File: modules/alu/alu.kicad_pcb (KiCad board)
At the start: 2 copper layers, 7 parts, among them Q1 2N3906, Q2 2N3904, Q3 2N3904

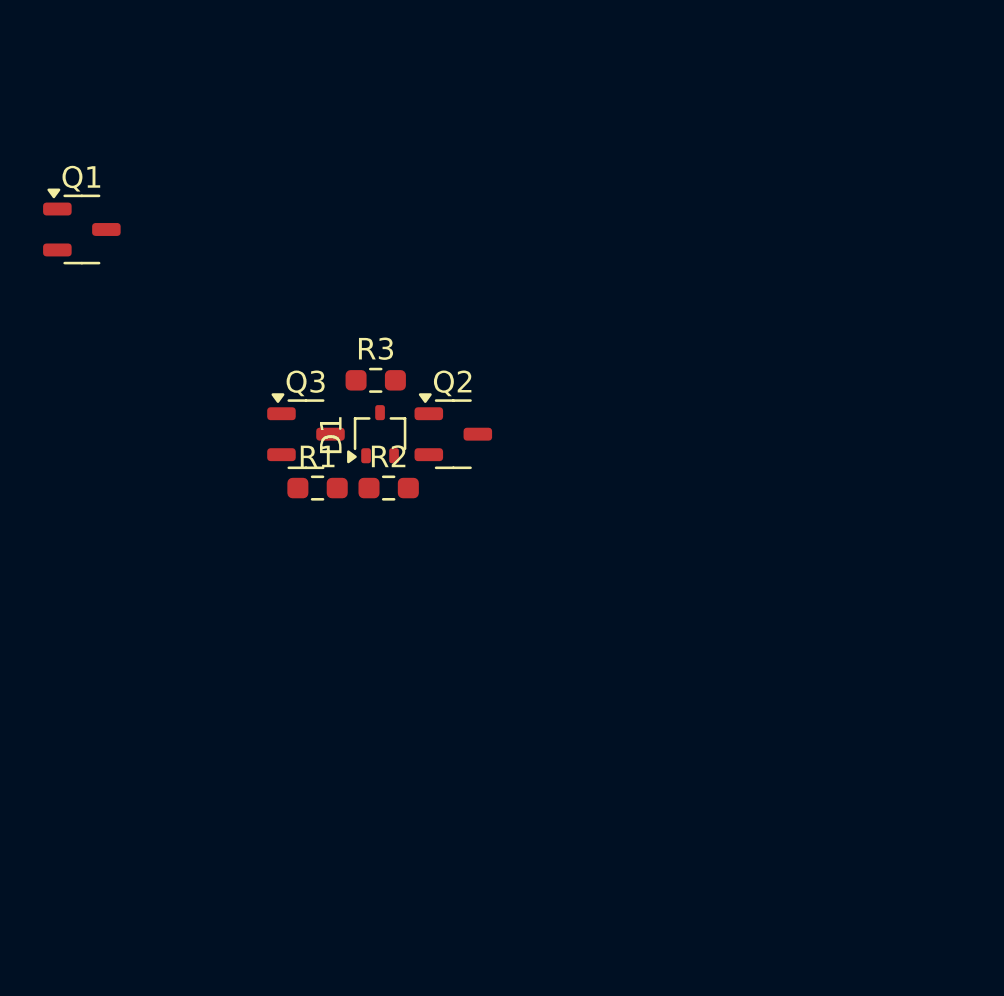
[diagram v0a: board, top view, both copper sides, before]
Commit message: Much work towards an actual ALU bit-cell.
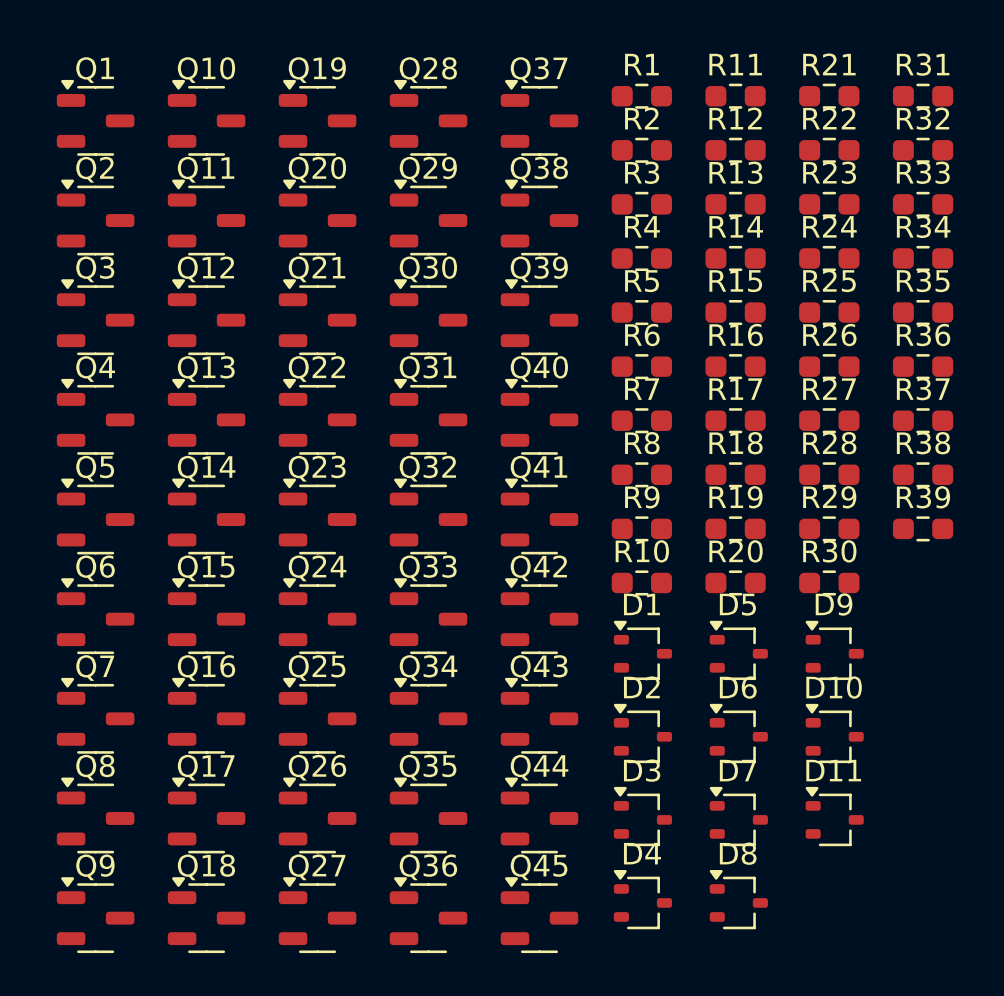
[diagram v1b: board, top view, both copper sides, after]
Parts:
- added D10: BAT54W, Package_TO_SOT_SMD:SOT-323_SC-70, F.Cu at (154.2, 96.6)
- added D11: BAT54W, Package_TO_SOT_SMD:SOT-323_SC-70, F.Cu at (154.2, 100.5)
- added D2: BAT54W, Package_TO_SOT_SMD:SOT-323_SC-70, F.Cu at (145.3, 96.6)
- added D3: BAT54W, Package_TO_SOT_SMD:SOT-323_SC-70, F.Cu at (145.3, 100.5)
- added D4: BAT54W, Package_TO_SOT_SMD:SOT-323_SC-70, F.Cu at (145.3, 104.4)
- added D5: BAT54W, Package_TO_SOT_SMD:SOT-323_SC-70, F.Cu at (149.8, 92.8)
- added D6: BAT54W, Package_TO_SOT_SMD:SOT-323_SC-70, F.Cu at (149.8, 96.6)
- added D7: BAT54W, Package_TO_SOT_SMD:SOT-323_SC-70, F.Cu at (149.8, 100.5)
- added D8: BAT54W, Package_TO_SOT_SMD:SOT-323_SC-70, F.Cu at (149.8, 104.4)
- added D9: BAT54W, Package_TO_SOT_SMD:SOT-323_SC-70, F.Cu at (154.2, 92.8)
- added Q10: 2N3906, Package_TO_SOT_SMD:SOT-23-3, F.Cu at (125.0, 68.1)
- added Q11: 2N3904, Package_TO_SOT_SMD:SOT-23-3, F.Cu at (125.0, 72.7)
- added Q12: 2N3904, Package_TO_SOT_SMD:SOT-23-3, F.Cu at (125.0, 77.3)
- added Q13: 2N3904, Package_TO_SOT_SMD:SOT-23-3, F.Cu at (125.0, 81.9)
- added Q14: 2N3904, Package_TO_SOT_SMD:SOT-23-3, F.Cu at (125.0, 86.6)
- added Q15: 2N3904, Package_TO_SOT_SMD:SOT-23-3, F.Cu at (125.0, 91.2)
- added Q16: 2N3904, Package_TO_SOT_SMD:SOT-23-3, F.Cu at (125.0, 95.8)
- added Q17: 2N3904, Package_TO_SOT_SMD:SOT-23-3, F.Cu at (125.0, 100.4)
- added Q18: 2N3906, Package_TO_SOT_SMD:SOT-23-3, F.Cu at (125.0, 105.1)
- added Q19: 2N3904, Package_TO_SOT_SMD:SOT-23-3, F.Cu at (130.2, 68.1)
- added Q20: 2N3906, Package_TO_SOT_SMD:SOT-23-3, F.Cu at (130.2, 72.7)
- added Q21: 2N3904, Package_TO_SOT_SMD:SOT-23-3, F.Cu at (130.2, 77.3)
- added Q22: 2N3906, Package_TO_SOT_SMD:SOT-23-3, F.Cu at (130.2, 81.9)
- added Q23: 2N3904, Package_TO_SOT_SMD:SOT-23-3, F.Cu at (130.2, 86.6)
- added Q24: 2N3906, Package_TO_SOT_SMD:SOT-23-3, F.Cu at (130.2, 91.2)
- added Q25: 2N3906, Package_TO_SOT_SMD:SOT-23-3, F.Cu at (130.2, 95.8)
- added Q26: 2N3906, Package_TO_SOT_SMD:SOT-23-3, F.Cu at (130.2, 100.4)
- added Q27: 2N3906, Package_TO_SOT_SMD:SOT-23-3, F.Cu at (130.2, 105.1)
- added Q28: 2N3904, Package_TO_SOT_SMD:SOT-23-3, F.Cu at (135.3, 68.1)
- added Q29: 2N3904, Package_TO_SOT_SMD:SOT-23-3, F.Cu at (135.3, 72.7)
- added Q30: 2N3904, Package_TO_SOT_SMD:SOT-23-3, F.Cu at (135.3, 77.3)
- added Q31: 2N3906, Package_TO_SOT_SMD:SOT-23-3, F.Cu at (135.3, 81.9)
- added Q32: 2N3906, Package_TO_SOT_SMD:SOT-23-3, F.Cu at (135.3, 86.6)
- added Q33: 2N3904, Package_TO_SOT_SMD:SOT-23-3, F.Cu at (135.3, 91.2)
- added Q34: 2N3904, Package_TO_SOT_SMD:SOT-23-3, F.Cu at (135.3, 95.8)
- added Q35: 2N3906, Package_TO_SOT_SMD:SOT-23-3, F.Cu at (135.3, 100.4)
- added Q36: 2N3904, Package_TO_SOT_SMD:SOT-23-3, F.Cu at (135.3, 105.1)
- added Q37: 2N3906, Package_TO_SOT_SMD:SOT-23-3, F.Cu at (140.5, 68.1)
- added Q38: 2N3906, Package_TO_SOT_SMD:SOT-23-3, F.Cu at (140.5, 72.7)
- added Q39: 2N3906, Package_TO_SOT_SMD:SOT-23-3, F.Cu at (140.5, 77.3)
- added Q4: 2N3904, Package_TO_SOT_SMD:SOT-23-3, F.Cu at (119.9, 81.9)
- added Q40: 2N3906, Package_TO_SOT_SMD:SOT-23-3, F.Cu at (140.5, 81.9)
- added Q41: 2N3906, Package_TO_SOT_SMD:SOT-23-3, F.Cu at (140.5, 86.6)
- added Q42: 2N3906, Package_TO_SOT_SMD:SOT-23-3, F.Cu at (140.5, 91.2)
- added Q43: 2N3904, Package_TO_SOT_SMD:SOT-23-3, F.Cu at (140.5, 95.8)
- added Q44: 2N3904, Package_TO_SOT_SMD:SOT-23-3, F.Cu at (140.5, 100.4)
- added Q45: 2N3904, Package_TO_SOT_SMD:SOT-23-3, F.Cu at (140.5, 105.1)
- added Q5: 2N3904, Package_TO_SOT_SMD:SOT-23-3, F.Cu at (119.9, 86.6)
- added Q6: 2N3904, Package_TO_SOT_SMD:SOT-23-3, F.Cu at (119.9, 91.2)
- added Q7: 2N3906, Package_TO_SOT_SMD:SOT-23-3, F.Cu at (119.9, 95.8)
- added Q8: 2N3906, Package_TO_SOT_SMD:SOT-23-3, F.Cu at (119.9, 100.4)
- added Q9: 2N3906, Package_TO_SOT_SMD:SOT-23-3, F.Cu at (119.9, 105.1)
- added R10: 520, Resistor_SMD:R_0603_1608Metric_Pad0.98x0.95mm_HandSolder, F.Cu at (145.2, 89.5)
- added R11: 220, Resistor_SMD:R_0603_1608Metric_Pad0.98x0.95mm_HandSolder, F.Cu at (149.6, 66.9)
- added R12: 220, Resistor_SMD:R_0603_1608Metric_Pad0.98x0.95mm_HandSolder, F.Cu at (149.6, 69.4)
- added R13: 220, Resistor_SMD:R_0603_1608Metric_Pad0.98x0.95mm_HandSolder, F.Cu at (149.6, 71.9)
- added R14: 220, Resistor_SMD:R_0603_1608Metric_Pad0.98x0.95mm_HandSolder, F.Cu at (149.6, 74.4)
- added R15: 100, Resistor_SMD:R_0603_1608Metric_Pad0.98x0.95mm_HandSolder, F.Cu at (149.6, 77.0)
- added R16: 100, Resistor_SMD:R_0603_1608Metric_Pad0.98x0.95mm_HandSolder, F.Cu at (149.6, 79.5)
- added R17: 220, Resistor_SMD:R_0603_1608Metric_Pad0.98x0.95mm_HandSolder, F.Cu at (149.6, 82.0)
- added R18: 220, Resistor_SMD:R_0603_1608Metric_Pad0.98x0.95mm_HandSolder, F.Cu at (149.6, 84.5)
- added R19: 220, Resistor_SMD:R_0603_1608Metric_Pad0.98x0.95mm_HandSolder, F.Cu at (149.6, 87.0)
- added R20: 220, Resistor_SMD:R_0603_1608Metric_Pad0.98x0.95mm_HandSolder, F.Cu at (149.6, 89.5)
- added R21: 100, Resistor_SMD:R_0603_1608Metric_Pad0.98x0.95mm_HandSolder, F.Cu at (153.9, 66.9)
- added R22: 100, Resistor_SMD:R_0603_1608Metric_Pad0.98x0.95mm_HandSolder, F.Cu at (153.9, 69.4)
- added R23: 520, Resistor_SMD:R_0603_1608Metric_Pad0.98x0.95mm_HandSolder, F.Cu at (153.9, 71.9)
- added R24: 220, Resistor_SMD:R_0603_1608Metric_Pad0.98x0.95mm_HandSolder, F.Cu at (153.9, 74.4)
- added R25: 220, Resistor_SMD:R_0603_1608Metric_Pad0.98x0.95mm_HandSolder, F.Cu at (153.9, 77.0)
- added R26: 100, Resistor_SMD:R_0603_1608Metric_Pad0.98x0.95mm_HandSolder, F.Cu at (153.9, 79.5)
- added R27: 220, Resistor_SMD:R_0603_1608Metric_Pad0.98x0.95mm_HandSolder, F.Cu at (153.9, 82.0)
- added R28: 220, Resistor_SMD:R_0603_1608Metric_Pad0.98x0.95mm_HandSolder, F.Cu at (153.9, 84.5)
- added R29: 220, Resistor_SMD:R_0603_1608Metric_Pad0.98x0.95mm_HandSolder, F.Cu at (153.9, 87.0)
- added R30: 220, Resistor_SMD:R_0603_1608Metric_Pad0.98x0.95mm_HandSolder, F.Cu at (153.9, 89.5)
- added R31: 100, Resistor_SMD:R_0603_1608Metric_Pad0.98x0.95mm_HandSolder, F.Cu at (158.3, 66.9)
- added R32: 100, Resistor_SMD:R_0603_1608Metric_Pad0.98x0.95mm_HandSolder, F.Cu at (158.3, 69.4)
- added R33: 520, Resistor_SMD:R_0603_1608Metric_Pad0.98x0.95mm_HandSolder, F.Cu at (158.3, 71.9)
- added R34: 220, Resistor_SMD:R_0603_1608Metric_Pad0.98x0.95mm_HandSolder, F.Cu at (158.3, 74.4)
- added R35: 220, Resistor_SMD:R_0603_1608Metric_Pad0.98x0.95mm_HandSolder, F.Cu at (158.3, 77.0)
- added R36: 100, Resistor_SMD:R_0603_1608Metric_Pad0.98x0.95mm_HandSolder, F.Cu at (158.3, 79.5)
- added R37: 220, Resistor_SMD:R_0603_1608Metric_Pad0.98x0.95mm_HandSolder, F.Cu at (158.3, 82.0)
- added R38: 220, Resistor_SMD:R_0603_1608Metric_Pad0.98x0.95mm_HandSolder, F.Cu at (158.3, 84.5)
- added R39: 100, Resistor_SMD:R_0603_1608Metric_Pad0.98x0.95mm_HandSolder, F.Cu at (158.3, 87.0)
- added R4: 220, Resistor_SMD:R_0603_1608Metric_Pad0.98x0.95mm_HandSolder, F.Cu at (145.2, 74.4)
- added R5: 220, Resistor_SMD:R_0603_1608Metric_Pad0.98x0.95mm_HandSolder, F.Cu at (145.2, 77.0)
- added R6: 220, Resistor_SMD:R_0603_1608Metric_Pad0.98x0.95mm_HandSolder, F.Cu at (145.2, 79.5)
- added R7: 100, Resistor_SMD:R_0603_1608Metric_Pad0.98x0.95mm_HandSolder, F.Cu at (145.2, 82.0)
- added R8: 100, Resistor_SMD:R_0603_1608Metric_Pad0.98x0.95mm_HandSolder, F.Cu at (145.2, 84.5)
- added R9: 520, Resistor_SMD:R_0603_1608Metric_Pad0.98x0.95mm_HandSolder, F.Cu at (145.2, 87.0)
- Q1: value 2N3906 -> 2N3904
- R1: value 600 -> 10k
- R2: value 300 -> 10k
- R3: value 300 -> 220
- moved R1 23.6 mm to (145.2, 66.9)
- moved R2 19.6 mm to (145.2, 69.4)
- moved Q2 19.3 mm to (119.9, 72.7)
- moved D1 15.9 mm to (145.3, 92.8), turned to 0 degrees
- moved R3 14.8 mm to (145.2, 71.9)
- moved Q3 11.1 mm to (119.9, 77.3)
- moved Q1 5.08 mm to (119.9, 68.1)
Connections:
- D1 pad 1: /BASE -> Net-(D1-A)
- D1 pad 3: /OUT -> Net-(D1-K)
- Q1 pad 1: unconnected-(Q1-C-Pad1) -> VCC
- Q1 pad 2: unconnected-(Q1-B-Pad2) -> /IN_A0
- Q1 pad 3: unconnected-(Q1-E-Pad3) -> Net-(Q1-E)
- Q2 pad 1: /OUT -> VCC
- Q2 pad 2: /BASE -> /IN_B0
- Q2 pad 3: 0 -> Net-(Q2-E)
- Q3 pad 2: /IN -> /IN_INV_A
- Q3 pad 3: Net-(Q3-E) -> Net-(Q1-E)
- R1 pad 1: Net-(Q3-E) -> /IN_INV_A
- R1 pad 2: /BASE -> 0
- R2 pad 1: /BASE -> /IN_INV_B
- R3 pad 1: VCC -> Net-(Q1-E)
- R3 pad 2: /OUT -> Net-(D1-A)

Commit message: Small ALU fix.
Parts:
- added D100: BAT54W, Package_TO_SOT_SMD:SOT-323_SC-70, F.Cu at (73.8, 3.92)
- added D101: BAT54W, Package_TO_SOT_SMD:SOT-323_SC-70, F.Cu at (60.5, 39.8)
- added D102: BAT54W, Package_TO_SOT_SMD:SOT-323_SC-70, F.Cu at (60.5, 43.7)
- added D103: BAT54W, Package_TO_SOT_SMD:SOT-323_SC-70, F.Cu at (60.5, 47.5)
- added D104: BAT54W, Package_TO_SOT_SMD:SOT-323_SC-70, F.Cu at (65.0, 39.8)
- added D105: BAT54W, Package_TO_SOT_SMD:SOT-323_SC-70, F.Cu at (65.0, 43.7)
- added D106: BAT54W, Package_TO_SOT_SMD:SOT-323_SC-70, F.Cu at (65.0, 47.5)
- added D107: BAT54W, Package_TO_SOT_SMD:SOT-323_SC-70, F.Cu at (69.4, 39.8)
- added D108: BAT54W, Package_TO_SOT_SMD:SOT-323_SC-70, F.Cu at (69.4, 43.7)
- added D109: BAT54W, Package_TO_SOT_SMD:SOT-323_SC-70, F.Cu at (69.4, 47.5)
- added D110: BAT54W, Package_TO_SOT_SMD:SOT-323_SC-70, F.Cu at (73.8, 39.8)
- added D111: BAT54W, Package_TO_SOT_SMD:SOT-323_SC-70, F.Cu at (73.8, 43.7)
- added D112: BAT54W, Package_TO_SOT_SMD:SOT-323_SC-70, F.Cu at (73.8, 47.5)
- added D113: BAT54W, Package_TO_SOT_SMD:SOT-323_SC-70, F.Cu at (248.2, 109.5)
- added D114: BAT54W, Package_TO_SOT_SMD:SOT-323_SC-70, F.Cu at (248.2, 113.4)
- added D115: BAT54W, Package_TO_SOT_SMD:SOT-323_SC-70, F.Cu at (248.2, 117.2)
- added D116: BAT54W, Package_TO_SOT_SMD:SOT-323_SC-70, F.Cu at (248.2, 121.1)
- added D117: BAT54W, Package_TO_SOT_SMD:SOT-323_SC-70, F.Cu at (248.2, 124.9)
- added D118: BAT54W, Package_TO_SOT_SMD:SOT-323_SC-70, F.Cu at (252.7, 109.5)
- added D119: BAT54W, Package_TO_SOT_SMD:SOT-323_SC-70, F.Cu at (252.7, 113.4)
- added D12: BAT54W, Package_TO_SOT_SMD:SOT-323_SC-70, F.Cu at (124.0, 83.5)
- added D120: BAT54W, Package_TO_SOT_SMD:SOT-323_SC-70, F.Cu at (252.7, 117.2)
- added D121: BAT54W, Package_TO_SOT_SMD:SOT-323_SC-70, F.Cu at (178.5, 83.5)
- added D122: BAT54W, Package_TO_SOT_SMD:SOT-323_SC-70, F.Cu at (178.5, 87.3)
- added D123: BAT54W, Package_TO_SOT_SMD:SOT-323_SC-70, F.Cu at (178.5, 91.2)
- added D124: BAT54W, Package_TO_SOT_SMD:SOT-323_SC-70, F.Cu at (182.9, 83.5)
- added D125: BAT54W, Package_TO_SOT_SMD:SOT-323_SC-70, F.Cu at (182.9, 87.3)
- added D126: BAT54W, Package_TO_SOT_SMD:SOT-323_SC-70, F.Cu at (182.9, 91.2)
- added D127: BAT54W, Package_TO_SOT_SMD:SOT-323_SC-70, F.Cu at (187.4, 83.5)
- added D128: BAT54W, Package_TO_SOT_SMD:SOT-323_SC-70, F.Cu at (187.4, 87.3)
- added D129: BAT54W, Package_TO_SOT_SMD:SOT-323_SC-70, F.Cu at (187.4, 91.2)
- added D13: BAT54W, Package_TO_SOT_SMD:SOT-323_SC-70, F.Cu at (124.0, 87.3)
- added D130: BAT54W, Package_TO_SOT_SMD:SOT-323_SC-70, F.Cu at (191.8, 83.5)
- added D131: BAT54W, Package_TO_SOT_SMD:SOT-323_SC-70, F.Cu at (191.8, 87.3)
- added D132: BAT54W, Package_TO_SOT_SMD:SOT-323_SC-70, F.Cu at (191.8, 91.2)
- added D133: BAT54W, Package_TO_SOT_SMD:SOT-323_SC-70, F.Cu at (119.5, 127.1)
- added D134: BAT54W, Package_TO_SOT_SMD:SOT-323_SC-70, F.Cu at (119.5, 130.9)
- added D135: BAT54W, Package_TO_SOT_SMD:SOT-323_SC-70, F.Cu at (119.5, 134.8)
- added D136: BAT54W, Package_TO_SOT_SMD:SOT-323_SC-70, F.Cu at (124.0, 127.1)
- added D137: BAT54W, Package_TO_SOT_SMD:SOT-323_SC-70, F.Cu at (124.0, 130.9)
- added D138: BAT54W, Package_TO_SOT_SMD:SOT-323_SC-70, F.Cu at (124.0, 134.8)
- added D139: BAT54W, Package_TO_SOT_SMD:SOT-323_SC-70, F.Cu at (128.4, 127.1)
- added D14: BAT54W, Package_TO_SOT_SMD:SOT-323_SC-70, F.Cu at (124.0, 91.2)
- added D140: BAT54W, Package_TO_SOT_SMD:SOT-323_SC-70, F.Cu at (128.4, 130.9)
- added D141: BAT54W, Package_TO_SOT_SMD:SOT-323_SC-70, F.Cu at (128.4, 134.8)
- added D142: BAT54W, Package_TO_SOT_SMD:SOT-323_SC-70, F.Cu at (132.8, 127.1)
- added D143: BAT54W, Package_TO_SOT_SMD:SOT-323_SC-70, F.Cu at (132.8, 130.9)
- added D144: BAT54W, Package_TO_SOT_SMD:SOT-323_SC-70, F.Cu at (132.8, 134.8)
- added D145: BAT54W, Package_TO_SOT_SMD:SOT-323_SC-70, F.Cu at (237.5, 39.8)
- added D146: BAT54W, Package_TO_SOT_SMD:SOT-323_SC-70, F.Cu at (237.5, 43.7)
- added D147: BAT54W, Package_TO_SOT_SMD:SOT-323_SC-70, F.Cu at (237.5, 47.5)
- added D148: BAT54W, Package_TO_SOT_SMD:SOT-323_SC-70, F.Cu at (241.9, 39.8)
- added D149: BAT54W, Package_TO_SOT_SMD:SOT-323_SC-70, F.Cu at (241.9, 43.7)
- added D15: BAT54W, Package_TO_SOT_SMD:SOT-323_SC-70, F.Cu at (128.4, 83.5)
- added D150: BAT54W, Package_TO_SOT_SMD:SOT-323_SC-70, F.Cu at (241.9, 47.5)
- added D151: BAT54W, Package_TO_SOT_SMD:SOT-323_SC-70, F.Cu at (246.4, 39.8)
- added D152: BAT54W, Package_TO_SOT_SMD:SOT-323_SC-70, F.Cu at (246.4, 43.7)
- added D153: BAT54W, Package_TO_SOT_SMD:SOT-323_SC-70, F.Cu at (246.4, 47.5)
- added D154: BAT54W, Package_TO_SOT_SMD:SOT-323_SC-70, F.Cu at (250.8, 39.8)
- added D155: BAT54W, Package_TO_SOT_SMD:SOT-323_SC-70, F.Cu at (250.8, 43.7)
- added D156: BAT54W, Package_TO_SOT_SMD:SOT-323_SC-70, F.Cu at (250.8, 47.5)
- added D157: BAT54W, Package_TO_SOT_SMD:SOT-323_SC-70, F.Cu at (178.5, 39.8)
- added D158: BAT54W, Package_TO_SOT_SMD:SOT-323_SC-70, F.Cu at (178.5, 43.7)
- added D159: BAT54W, Package_TO_SOT_SMD:SOT-323_SC-70, F.Cu at (178.5, 47.5)
- added D16: BAT54W, Package_TO_SOT_SMD:SOT-323_SC-70, F.Cu at (128.4, 87.3)
- added D160: BAT54W, Package_TO_SOT_SMD:SOT-323_SC-70, F.Cu at (182.9, 39.8)
- added D161: BAT54W, Package_TO_SOT_SMD:SOT-323_SC-70, F.Cu at (182.9, 43.7)
- added D162: BAT54W, Package_TO_SOT_SMD:SOT-323_SC-70, F.Cu at (182.9, 47.5)
- added D163: BAT54W, Package_TO_SOT_SMD:SOT-323_SC-70, F.Cu at (187.4, 39.8)
- added D164: BAT54W, Package_TO_SOT_SMD:SOT-323_SC-70, F.Cu at (187.4, 43.7)
- added D165: BAT54W, Package_TO_SOT_SMD:SOT-323_SC-70, F.Cu at (187.4, 47.5)
- added D166: BAT54W, Package_TO_SOT_SMD:SOT-323_SC-70, F.Cu at (191.8, 39.8)
- added D167: BAT54W, Package_TO_SOT_SMD:SOT-323_SC-70, F.Cu at (191.8, 43.7)
- added D168: BAT54W, Package_TO_SOT_SMD:SOT-323_SC-70, F.Cu at (191.8, 47.5)
- added D169: BAT54W, Package_TO_SOT_SMD:SOT-323_SC-70, F.Cu at (227.2, 65.9)
- added D17: BAT54W, Package_TO_SOT_SMD:SOT-323_SC-70, F.Cu at (128.4, 91.2)
- added D170: BAT54W, Package_TO_SOT_SMD:SOT-323_SC-70, F.Cu at (227.2, 69.7)
- added D171: BAT54W, Package_TO_SOT_SMD:SOT-323_SC-70, F.Cu at (227.2, 73.6)
- added D172: BAT54W, Package_TO_SOT_SMD:SOT-323_SC-70, F.Cu at (227.2, 77.5)
- added D173: BAT54W, Package_TO_SOT_SMD:SOT-323_SC-70, F.Cu at (227.2, 81.3)
- added D174: BAT54W, Package_TO_SOT_SMD:SOT-323_SC-70, F.Cu at (231.7, 65.9)
- added D175: BAT54W, Package_TO_SOT_SMD:SOT-323_SC-70, F.Cu at (231.7, 69.7)
- added D176: BAT54W, Package_TO_SOT_SMD:SOT-323_SC-70, F.Cu at (231.7, 73.6)
- added D177: BAT54W, Package_TO_SOT_SMD:SOT-323_SC-70, F.Cu at (178.5, -3.79)
- added D178: BAT54W, Package_TO_SOT_SMD:SOT-323_SC-70, F.Cu at (178.5, 0.07)
- added D179: BAT54W, Package_TO_SOT_SMD:SOT-323_SC-70, F.Cu at (178.5, 3.92)
- added D18: BAT54W, Package_TO_SOT_SMD:SOT-323_SC-70, F.Cu at (132.8, 83.5)
- added D180: BAT54W, Package_TO_SOT_SMD:SOT-323_SC-70, F.Cu at (182.9, -3.79)
- added D181: BAT54W, Package_TO_SOT_SMD:SOT-323_SC-70, F.Cu at (182.9, 0.07)
- added D182: BAT54W, Package_TO_SOT_SMD:SOT-323_SC-70, F.Cu at (182.9, 3.92)
- added D183: BAT54W, Package_TO_SOT_SMD:SOT-323_SC-70, F.Cu at (187.4, -3.79)
- added D184: BAT54W, Package_TO_SOT_SMD:SOT-323_SC-70, F.Cu at (187.4, 0.07)
- added D185: BAT54W, Package_TO_SOT_SMD:SOT-323_SC-70, F.Cu at (187.4, 3.92)
- added D186: BAT54W, Package_TO_SOT_SMD:SOT-323_SC-70, F.Cu at (191.8, -3.79)
- added D187: BAT54W, Package_TO_SOT_SMD:SOT-323_SC-70, F.Cu at (191.8, 0.07)
- added D188: BAT54W, Package_TO_SOT_SMD:SOT-323_SC-70, F.Cu at (191.8, 3.92)
- added D189: BAT54W, Package_TO_SOT_SMD:SOT-323_SC-70, F.Cu at (60.5, 83.5)
- added D19: BAT54W, Package_TO_SOT_SMD:SOT-323_SC-70, F.Cu at (132.8, 87.3)
- added D190: BAT54W, Package_TO_SOT_SMD:SOT-323_SC-70, F.Cu at (60.5, 87.3)
- added D191: BAT54W, Package_TO_SOT_SMD:SOT-323_SC-70, F.Cu at (60.5, 91.2)
- added D192: BAT54W, Package_TO_SOT_SMD:SOT-323_SC-70, F.Cu at (65.0, 83.5)
- added D193: BAT54W, Package_TO_SOT_SMD:SOT-323_SC-70, F.Cu at (65.0, 87.3)
- added D194: BAT54W, Package_TO_SOT_SMD:SOT-323_SC-70, F.Cu at (65.0, 91.2)
- added D195: BAT54W, Package_TO_SOT_SMD:SOT-323_SC-70, F.Cu at (69.4, 83.5)
- added D196: BAT54W, Package_TO_SOT_SMD:SOT-323_SC-70, F.Cu at (69.4, 87.3)
- added D197: BAT54W, Package_TO_SOT_SMD:SOT-323_SC-70, F.Cu at (69.4, 91.2)
- added D198: BAT54W, Package_TO_SOT_SMD:SOT-323_SC-70, F.Cu at (73.8, 83.5)
- added D199: BAT54W, Package_TO_SOT_SMD:SOT-323_SC-70, F.Cu at (73.8, 87.3)
- added D20: BAT54W, Package_TO_SOT_SMD:SOT-323_SC-70, F.Cu at (132.8, 91.2)
- added D200: BAT54W, Package_TO_SOT_SMD:SOT-323_SC-70, F.Cu at (73.8, 91.2)
- added D201: BAT54W, Package_TO_SOT_SMD:SOT-323_SC-70, F.Cu at (119.5, -3.79)
- added D202: BAT54W, Package_TO_SOT_SMD:SOT-323_SC-70, F.Cu at (119.5, 0.07)
- added D203: BAT54W, Package_TO_SOT_SMD:SOT-323_SC-70, F.Cu at (119.5, 3.92)
- added D204: BAT54W, Package_TO_SOT_SMD:SOT-323_SC-70, F.Cu at (124.0, -3.79)
- added D205: BAT54W, Package_TO_SOT_SMD:SOT-323_SC-70, F.Cu at (124.0, 0.07)
- added D206: BAT54W, Package_TO_SOT_SMD:SOT-323_SC-70, F.Cu at (124.0, 3.92)
- added D207: BAT54W, Package_TO_SOT_SMD:SOT-323_SC-70, F.Cu at (128.4, -3.79)
- added D208: BAT54W, Package_TO_SOT_SMD:SOT-323_SC-70, F.Cu at (128.4, 0.07)
- added D209: BAT54W, Package_TO_SOT_SMD:SOT-323_SC-70, F.Cu at (128.4, 3.92)
- added D21: BAT54W, Package_TO_SOT_SMD:SOT-323_SC-70, F.Cu at (110.8, -47.6)
- added D210: BAT54W, Package_TO_SOT_SMD:SOT-323_SC-70, F.Cu at (132.8, -3.79)
- added D211: BAT54W, Package_TO_SOT_SMD:SOT-323_SC-70, F.Cu at (132.8, 0.07)
- added D212: BAT54W, Package_TO_SOT_SMD:SOT-323_SC-70, F.Cu at (132.8, 3.92)
- added D213: BAT54W, Package_TO_SOT_SMD:SOT-323_SC-70, F.Cu at (60.5, 127.1)
- added D214: BAT54W, Package_TO_SOT_SMD:SOT-323_SC-70, F.Cu at (60.5, 130.9)
- added D215: BAT54W, Package_TO_SOT_SMD:SOT-323_SC-70, F.Cu at (60.5, 134.8)
- added D216: BAT54W, Package_TO_SOT_SMD:SOT-323_SC-70, F.Cu at (65.0, 127.1)
- added D217: BAT54W, Package_TO_SOT_SMD:SOT-323_SC-70, F.Cu at (65.0, 130.9)
- added D218: BAT54W, Package_TO_SOT_SMD:SOT-323_SC-70, F.Cu at (65.0, 134.8)
- added D219: BAT54W, Package_TO_SOT_SMD:SOT-323_SC-70, F.Cu at (69.4, 127.1)
- added D22: BAT54W, Package_TO_SOT_SMD:SOT-323_SC-70, F.Cu at (110.8, -43.8)
- added D220: BAT54W, Package_TO_SOT_SMD:SOT-323_SC-70, F.Cu at (69.4, 130.9)
- added D221: BAT54W, Package_TO_SOT_SMD:SOT-323_SC-70, F.Cu at (69.4, 134.8)
- added D222: BAT54W, Package_TO_SOT_SMD:SOT-323_SC-70, F.Cu at (73.8, 127.1)
- added D223: BAT54W, Package_TO_SOT_SMD:SOT-323_SC-70, F.Cu at (73.8, 130.9)
- added D224: BAT54W, Package_TO_SOT_SMD:SOT-323_SC-70, F.Cu at (73.8, 134.8)
- added D225: BAT54W, Package_TO_SOT_SMD:SOT-323_SC-70, F.Cu at (60.5, -42.6)
- added D226: BAT54W, Package_TO_SOT_SMD:SOT-323_SC-70, F.Cu at (60.5, -38.8)
- added D227: BAT54W, Package_TO_SOT_SMD:SOT-323_SC-70, F.Cu at (60.5, -34.9)
- added D228: BAT54W, Package_TO_SOT_SMD:SOT-323_SC-70, F.Cu at (60.5, -31.1)
- added D229: BAT54W, Package_TO_SOT_SMD:SOT-323_SC-70, F.Cu at (60.5, -27.2)
- added D23: BAT54W, Package_TO_SOT_SMD:SOT-323_SC-70, F.Cu at (110.8, -39.9)
- added D230: BAT54W, Package_TO_SOT_SMD:SOT-323_SC-70, F.Cu at (65.0, -42.6)
- added D231: BAT54W, Package_TO_SOT_SMD:SOT-323_SC-70, F.Cu at (65.0, -38.8)
- added D232: BAT54W, Package_TO_SOT_SMD:SOT-323_SC-70, F.Cu at (65.0, -34.9)
- added D233: BAT54W, Package_TO_SOT_SMD:SOT-323_SC-70, F.Cu at (65.0, -31.1)
- added D234: BAT54W, Package_TO_SOT_SMD:SOT-323_SC-70, F.Cu at (65.0, -27.2)
- added D24: BAT54W, Package_TO_SOT_SMD:SOT-323_SC-70, F.Cu at (115.2, -47.6)
- added D25: BAT54W, Package_TO_SOT_SMD:SOT-323_SC-70, F.Cu at (115.2, -43.8)
- added D26: BAT54W, Package_TO_SOT_SMD:SOT-323_SC-70, F.Cu at (115.2, -39.9)
- added D27: BAT54W, Package_TO_SOT_SMD:SOT-323_SC-70, F.Cu at (119.7, -47.6)
- added D28: BAT54W, Package_TO_SOT_SMD:SOT-323_SC-70, F.Cu at (119.7, -43.8)
- added D29: BAT54W, Package_TO_SOT_SMD:SOT-323_SC-70, F.Cu at (119.7, -39.9)
- added D30: BAT54W, Package_TO_SOT_SMD:SOT-323_SC-70, F.Cu at (124.2, -47.6)
- added D31: BAT54W, Package_TO_SOT_SMD:SOT-323_SC-70, F.Cu at (124.2, -43.8)
- added D32: BAT54W, Package_TO_SOT_SMD:SOT-323_SC-70, F.Cu at (124.2, -39.9)
- added D33: BAT54W, Package_TO_SOT_SMD:SOT-323_SC-70, F.Cu at (119.5, 39.8)
- added D34: BAT54W, Package_TO_SOT_SMD:SOT-323_SC-70, F.Cu at (119.5, 43.7)
- added D35: BAT54W, Package_TO_SOT_SMD:SOT-323_SC-70, F.Cu at (119.5, 47.5)
- added D36: BAT54W, Package_TO_SOT_SMD:SOT-323_SC-70, F.Cu at (124.0, 39.8)
- added D37: BAT54W, Package_TO_SOT_SMD:SOT-323_SC-70, F.Cu at (124.0, 43.7)
- added D38: BAT54W, Package_TO_SOT_SMD:SOT-323_SC-70, F.Cu at (124.0, 47.5)
- added D39: BAT54W, Package_TO_SOT_SMD:SOT-323_SC-70, F.Cu at (128.4, 39.8)
- added D40: BAT54W, Package_TO_SOT_SMD:SOT-323_SC-70, F.Cu at (128.4, 43.7)
- added D41: BAT54W, Package_TO_SOT_SMD:SOT-323_SC-70, F.Cu at (128.4, 47.5)
- added D42: BAT54W, Package_TO_SOT_SMD:SOT-323_SC-70, F.Cu at (132.8, 39.8)
- added D43: BAT54W, Package_TO_SOT_SMD:SOT-323_SC-70, F.Cu at (132.8, 43.7)
- added D44: BAT54W, Package_TO_SOT_SMD:SOT-323_SC-70, F.Cu at (132.8, 47.5)
- added D45: BAT54W, Package_TO_SOT_SMD:SOT-323_SC-70, F.Cu at (237.5, -3.79)
- added D46: BAT54W, Package_TO_SOT_SMD:SOT-323_SC-70, F.Cu at (237.5, 0.07)
- added D47: BAT54W, Package_TO_SOT_SMD:SOT-323_SC-70, F.Cu at (237.5, 3.92)
- added D48: BAT54W, Package_TO_SOT_SMD:SOT-323_SC-70, F.Cu at (241.9, -3.79)
- added D49: BAT54W, Package_TO_SOT_SMD:SOT-323_SC-70, F.Cu at (241.9, 0.07)
- added D50: BAT54W, Package_TO_SOT_SMD:SOT-323_SC-70, F.Cu at (241.9, 3.92)
- added D51: BAT54W, Package_TO_SOT_SMD:SOT-323_SC-70, F.Cu at (246.4, -3.79)
- added D52: BAT54W, Package_TO_SOT_SMD:SOT-323_SC-70, F.Cu at (246.4, 0.07)
- added D53: BAT54W, Package_TO_SOT_SMD:SOT-323_SC-70, F.Cu at (246.4, 3.92)
- added D54: BAT54W, Package_TO_SOT_SMD:SOT-323_SC-70, F.Cu at (250.8, -3.79)
- added D55: BAT54W, Package_TO_SOT_SMD:SOT-323_SC-70, F.Cu at (250.8, 0.07)
- added D56: BAT54W, Package_TO_SOT_SMD:SOT-323_SC-70, F.Cu at (250.8, 3.92)
- added D57: BAT54W, Package_TO_SOT_SMD:SOT-323_SC-70, F.Cu at (208.2, 109.5)
- added D58: BAT54W, Package_TO_SOT_SMD:SOT-323_SC-70, F.Cu at (208.2, 113.4)
- added D59: BAT54W, Package_TO_SOT_SMD:SOT-323_SC-70, F.Cu at (208.2, 117.2)
- added D60: BAT54W, Package_TO_SOT_SMD:SOT-323_SC-70, F.Cu at (208.2, 121.1)
- added D61: BAT54W, Package_TO_SOT_SMD:SOT-323_SC-70, F.Cu at (208.2, 124.9)
- added D62: BAT54W, Package_TO_SOT_SMD:SOT-323_SC-70, F.Cu at (212.7, 109.5)
- added D63: BAT54W, Package_TO_SOT_SMD:SOT-323_SC-70, F.Cu at (212.7, 113.4)
- added D64: BAT54W, Package_TO_SOT_SMD:SOT-323_SC-70, F.Cu at (212.7, 117.2)
- added D65: BAT54W, Package_TO_SOT_SMD:SOT-323_SC-70, F.Cu at (228.8, -47.6)
- added D66: BAT54W, Package_TO_SOT_SMD:SOT-323_SC-70, F.Cu at (228.8, -43.8)
- added D67: BAT54W, Package_TO_SOT_SMD:SOT-323_SC-70, F.Cu at (228.8, -39.9)
- added D68: BAT54W, Package_TO_SOT_SMD:SOT-323_SC-70, F.Cu at (233.2, -47.6)
- added D69: BAT54W, Package_TO_SOT_SMD:SOT-323_SC-70, F.Cu at (233.2, -43.8)
- added D70: BAT54W, Package_TO_SOT_SMD:SOT-323_SC-70, F.Cu at (233.2, -39.9)
- added D71: BAT54W, Package_TO_SOT_SMD:SOT-323_SC-70, F.Cu at (237.7, -47.6)
- added D72: BAT54W, Package_TO_SOT_SMD:SOT-323_SC-70, F.Cu at (237.7, -43.8)
- added D73: BAT54W, Package_TO_SOT_SMD:SOT-323_SC-70, F.Cu at (237.7, -39.9)
- added D74: BAT54W, Package_TO_SOT_SMD:SOT-323_SC-70, F.Cu at (242.2, -47.6)
- added D75: BAT54W, Package_TO_SOT_SMD:SOT-323_SC-70, F.Cu at (242.2, -43.8)
- added D76: BAT54W, Package_TO_SOT_SMD:SOT-323_SC-70, F.Cu at (242.2, -39.9)
- added D77: BAT54W, Package_TO_SOT_SMD:SOT-323_SC-70, F.Cu at (169.8, -47.6)
- added D78: BAT54W, Package_TO_SOT_SMD:SOT-323_SC-70, F.Cu at (169.8, -43.8)
- added D79: BAT54W, Package_TO_SOT_SMD:SOT-323_SC-70, F.Cu at (169.8, -39.9)
- added D80: BAT54W, Package_TO_SOT_SMD:SOT-323_SC-70, F.Cu at (174.2, -47.6)
- added D81: BAT54W, Package_TO_SOT_SMD:SOT-323_SC-70, F.Cu at (174.2, -43.8)
- added D82: BAT54W, Package_TO_SOT_SMD:SOT-323_SC-70, F.Cu at (174.2, -39.9)
- added D83: BAT54W, Package_TO_SOT_SMD:SOT-323_SC-70, F.Cu at (178.7, -47.6)
- added D84: BAT54W, Package_TO_SOT_SMD:SOT-323_SC-70, F.Cu at (178.7, -43.8)
- added D85: BAT54W, Package_TO_SOT_SMD:SOT-323_SC-70, F.Cu at (178.7, -39.9)
- added D86: BAT54W, Package_TO_SOT_SMD:SOT-323_SC-70, F.Cu at (183.2, -47.6)
- added D87: BAT54W, Package_TO_SOT_SMD:SOT-323_SC-70, F.Cu at (183.2, -43.8)
- added D88: BAT54W, Package_TO_SOT_SMD:SOT-323_SC-70, F.Cu at (183.2, -39.9)
- added D89: BAT54W, Package_TO_SOT_SMD:SOT-323_SC-70, F.Cu at (60.5, -3.79)
- added D90: BAT54W, Package_TO_SOT_SMD:SOT-323_SC-70, F.Cu at (60.5, 0.07)
- added D91: BAT54W, Package_TO_SOT_SMD:SOT-323_SC-70, F.Cu at (60.5, 3.92)
- added D92: BAT54W, Package_TO_SOT_SMD:SOT-323_SC-70, F.Cu at (65.0, -3.79)
- added D93: BAT54W, Package_TO_SOT_SMD:SOT-323_SC-70, F.Cu at (65.0, 0.07)
- added D94: BAT54W, Package_TO_SOT_SMD:SOT-323_SC-70, F.Cu at (65.0, 3.92)
- added D95: BAT54W, Package_TO_SOT_SMD:SOT-323_SC-70, F.Cu at (69.4, -3.79)
- added D96: BAT54W, Package_TO_SOT_SMD:SOT-323_SC-70, F.Cu at (69.4, 0.07)
- added D97: BAT54W, Package_TO_SOT_SMD:SOT-323_SC-70, F.Cu at (69.4, 3.92)
- added D98: BAT54W, Package_TO_SOT_SMD:SOT-323_SC-70, F.Cu at (73.8, -3.79)
- added D99: BAT54W, Package_TO_SOT_SMD:SOT-323_SC-70, F.Cu at (73.8, 0.07)
- added Q100: 2N3904, Package_TO_SOT_SMD:SOT-23-3, F.Cu at (90.5, -51.0)
- added Q101: 2N3904, Package_TO_SOT_SMD:SOT-23-3, F.Cu at (90.5, -46.3)
- added Q102: 2N3904, Package_TO_SOT_SMD:SOT-23-3, F.Cu at (90.5, -41.7)
- added Q103: 2N3906, Package_TO_SOT_SMD:SOT-23-3, F.Cu at (90.5, -37.1)
- added Q104: 2N3904, Package_TO_SOT_SMD:SOT-23-3, F.Cu at (90.5, -32.5)
- added Q105: 2N3906, Package_TO_SOT_SMD:SOT-23-3, F.Cu at (90.5, -27.8)
- added Q106: 2N3904, Package_TO_SOT_SMD:SOT-23-3, F.Cu at (95.7, -64.8)
- added Q107: 2N3906, Package_TO_SOT_SMD:SOT-23-3, F.Cu at (95.7, -60.2)
- added Q108: 2N3904, Package_TO_SOT_SMD:SOT-23-3, F.Cu at (95.7, -55.6)
- added Q109: 2N3906, Package_TO_SOT_SMD:SOT-23-3, F.Cu at (95.7, -51.0)
- added Q110: 2N3906, Package_TO_SOT_SMD:SOT-23-3, F.Cu at (95.7, -46.3)
- added Q111: 2N3906, Package_TO_SOT_SMD:SOT-23-3, F.Cu at (95.7, -41.7)
- added Q112: 2N3904, Package_TO_SOT_SMD:SOT-23-3, F.Cu at (95.7, -37.1)
- added Q113: 2N3906, Package_TO_SOT_SMD:SOT-23-3, F.Cu at (95.7, -32.5)
- added Q114: 2N3906, Package_TO_SOT_SMD:SOT-23-3, F.Cu at (95.7, -27.8)
- added Q115: 2N3906, Package_TO_SOT_SMD:SOT-23-3, F.Cu at (100.8, -64.8)
- added Q116: 2N3906, Package_TO_SOT_SMD:SOT-23-3, F.Cu at (100.8, -60.2)
- added Q117: 2N3904, Package_TO_SOT_SMD:SOT-23-3, F.Cu at (100.8, -55.6)
- added Q118: 2N3906, Package_TO_SOT_SMD:SOT-23-3, F.Cu at (100.8, -51.0)
- added Q119: 2N3906, Package_TO_SOT_SMD:SOT-23-3, F.Cu at (100.8, -46.3)
- added Q120: 2N3906, Package_TO_SOT_SMD:SOT-23-3, F.Cu at (100.8, -41.7)
- added Q121: 2N3906, Package_TO_SOT_SMD:SOT-23-3, F.Cu at (100.8, -37.1)
- added Q122: 2N3904, Package_TO_SOT_SMD:SOT-23-3, F.Cu at (100.8, -32.5)
- added Q123: 2N3904, Package_TO_SOT_SMD:SOT-23-3, F.Cu at (100.8, -27.8)
- added Q124: 2N3904, Package_TO_SOT_SMD:SOT-23-3, F.Cu at (106.0, -64.8)
- added Q125: 2N3904, Package_TO_SOT_SMD:SOT-23-3, F.Cu at (106.0, -60.2)
- added Q126: 2N3904, Package_TO_SOT_SMD:SOT-23-3, F.Cu at (106.0, -55.6)
- added Q127: 2N3904, Package_TO_SOT_SMD:SOT-23-3, F.Cu at (106.0, -51.0)
- added Q128: 2N3904, Package_TO_SOT_SMD:SOT-23-3, F.Cu at (106.0, -46.3)
- added Q129: 2N3904, Package_TO_SOT_SMD:SOT-23-3, F.Cu at (89.0, 22.6)
- added Q130: 2N3904, Package_TO_SOT_SMD:SOT-23-3, F.Cu at (89.0, 27.3)
- added Q131: 2N3904, Package_TO_SOT_SMD:SOT-23-3, F.Cu at (89.0, 31.9)
- added Q132: 2N3904, Package_TO_SOT_SMD:SOT-23-3, F.Cu at (89.0, 36.5)
- added Q133: 2N3904, Package_TO_SOT_SMD:SOT-23-3, F.Cu at (89.0, 41.1)
- added Q134: 2N3904, Package_TO_SOT_SMD:SOT-23-3, F.Cu at (89.0, 45.8)
- added Q135: 2N3904, Package_TO_SOT_SMD:SOT-23-3, F.Cu at (89.0, 50.4)
- added Q136: 2N3904, Package_TO_SOT_SMD:SOT-23-3, F.Cu at (89.0, 55.0)
- added Q137: 2N3906, Package_TO_SOT_SMD:SOT-23-3, F.Cu at (89.0, 59.6)
- added Q138: 2N3906, Package_TO_SOT_SMD:SOT-23-3, F.Cu at (94.1, 22.6)
- added Q139: 2N3906, Package_TO_SOT_SMD:SOT-23-3, F.Cu at (94.1, 27.3)
- added Q140: 2N3906, Package_TO_SOT_SMD:SOT-23-3, F.Cu at (94.1, 31.9)
- added Q141: 2N3904, Package_TO_SOT_SMD:SOT-23-3, F.Cu at (94.1, 36.5)
- added Q142: 2N3904, Package_TO_SOT_SMD:SOT-23-3, F.Cu at (94.1, 41.1)
- added Q143: 2N3904, Package_TO_SOT_SMD:SOT-23-3, F.Cu at (94.1, 45.8)
- added Q144: 2N3906, Package_TO_SOT_SMD:SOT-23-3, F.Cu at (94.1, 50.4)
- added Q145: 2N3904, Package_TO_SOT_SMD:SOT-23-3, F.Cu at (94.1, 55.0)
- added Q146: 2N3904, Package_TO_SOT_SMD:SOT-23-3, F.Cu at (94.1, 59.6)
- added Q147: 2N3906, Package_TO_SOT_SMD:SOT-23-3, F.Cu at (99.2, 22.6)
- added Q148: 2N3904, Package_TO_SOT_SMD:SOT-23-3, F.Cu at (99.2, 27.3)
- added Q149: 2N3904, Package_TO_SOT_SMD:SOT-23-3, F.Cu at (99.2, 31.9)
- added Q150: 2N3904, Package_TO_SOT_SMD:SOT-23-3, F.Cu at (99.2, 36.5)
- added Q151: 2N3904, Package_TO_SOT_SMD:SOT-23-3, F.Cu at (99.2, 41.1)
- added Q152: 2N3904, Package_TO_SOT_SMD:SOT-23-3, F.Cu at (99.2, 45.8)
- added Q153: 2N3906, Package_TO_SOT_SMD:SOT-23-3, F.Cu at (99.2, 50.4)
- added Q154: 2N3904, Package_TO_SOT_SMD:SOT-23-3, F.Cu at (99.2, 55.0)
- added Q155: 2N3906, Package_TO_SOT_SMD:SOT-23-3, F.Cu at (99.2, 59.6)
- added Q156: 2N3904, Package_TO_SOT_SMD:SOT-23-3, F.Cu at (104.4, 22.6)
- added Q157: 2N3906, Package_TO_SOT_SMD:SOT-23-3, F.Cu at (104.4, 27.3)
- added Q158: 2N3904, Package_TO_SOT_SMD:SOT-23-3, F.Cu at (104.4, 31.9)
- added Q159: 2N3906, Package_TO_SOT_SMD:SOT-23-3, F.Cu at (104.4, 36.5)
- added Q160: 2N3906, Package_TO_SOT_SMD:SOT-23-3, F.Cu at (104.4, 41.1)
- added Q161: 2N3906, Package_TO_SOT_SMD:SOT-23-3, F.Cu at (104.4, 45.8)
- added Q162: 2N3904, Package_TO_SOT_SMD:SOT-23-3, F.Cu at (104.4, 50.4)
- added Q163: 2N3906, Package_TO_SOT_SMD:SOT-23-3, F.Cu at (104.4, 55.0)
- added Q164: 2N3906, Package_TO_SOT_SMD:SOT-23-3, F.Cu at (104.4, 59.6)
- added Q165: 2N3906, Package_TO_SOT_SMD:SOT-23-3, F.Cu at (109.5, 22.6)
- added Q166: 2N3906, Package_TO_SOT_SMD:SOT-23-3, F.Cu at (109.5, 27.3)
- added Q167: 2N3904, Package_TO_SOT_SMD:SOT-23-3, F.Cu at (109.5, 31.9)
- added Q168: 2N3906, Package_TO_SOT_SMD:SOT-23-3, F.Cu at (109.5, 36.5)
- added Q169: 2N3906, Package_TO_SOT_SMD:SOT-23-3, F.Cu at (109.5, 41.1)
- added Q170: 2N3906, Package_TO_SOT_SMD:SOT-23-3, F.Cu at (109.5, 45.8)
- added Q171: 2N3906, Package_TO_SOT_SMD:SOT-23-3, F.Cu at (109.5, 50.4)
- added Q172: 2N3904, Package_TO_SOT_SMD:SOT-23-3, F.Cu at (109.5, 55.0)
- added Q173: 2N3904, Package_TO_SOT_SMD:SOT-23-3, F.Cu at (109.5, 59.6)
- added Q174: 2N3904, Package_TO_SOT_SMD:SOT-23-3, F.Cu at (114.7, 22.6)
- added Q175: 2N3904, Package_TO_SOT_SMD:SOT-23-3, F.Cu at (114.7, 27.3)
- added Q176: 2N3904, Package_TO_SOT_SMD:SOT-23-3, F.Cu at (114.7, 31.9)
- added Q177: 2N3904, Package_TO_SOT_SMD:SOT-23-3, F.Cu at (114.7, 36.5)
- added Q178: 2N3904, Package_TO_SOT_SMD:SOT-23-3, F.Cu at (114.7, 41.1)
- added Q179: 2N3904, Package_TO_SOT_SMD:SOT-23-3, F.Cu at (206.9, -21.0)
- added Q180: 2N3904, Package_TO_SOT_SMD:SOT-23-3, F.Cu at (206.9, -16.4)
- added Q181: 2N3904, Package_TO_SOT_SMD:SOT-23-3, F.Cu at (206.9, -11.7)
- added Q182: 2N3904, Package_TO_SOT_SMD:SOT-23-3, F.Cu at (206.9, -7.11)
- added Q183: 2N3904, Package_TO_SOT_SMD:SOT-23-3, F.Cu at (206.9, -2.48)
- added Q184: 2N3904, Package_TO_SOT_SMD:SOT-23-3, F.Cu at (206.9, 2.14)
- added Q185: 2N3904, Package_TO_SOT_SMD:SOT-23-3, F.Cu at (206.9, 6.76)
- added Q186: 2N3904, Package_TO_SOT_SMD:SOT-23-3, F.Cu at (206.9, 11.4)
- added Q187: 2N3906, Package_TO_SOT_SMD:SOT-23-3, F.Cu at (206.9, 16.0)
- added Q188: 2N3906, Package_TO_SOT_SMD:SOT-23-3, F.Cu at (212.1, -21.0)
- added Q189: 2N3906, Package_TO_SOT_SMD:SOT-23-3, F.Cu at (212.1, -16.4)
- added Q190: 2N3906, Package_TO_SOT_SMD:SOT-23-3, F.Cu at (212.1, -11.7)
- added Q191: 2N3904, Package_TO_SOT_SMD:SOT-23-3, F.Cu at (212.1, -7.11)
- added Q192: 2N3904, Package_TO_SOT_SMD:SOT-23-3, F.Cu at (212.1, -2.48)
- added Q193: 2N3904, Package_TO_SOT_SMD:SOT-23-3, F.Cu at (212.1, 2.14)
- added Q194: 2N3906, Package_TO_SOT_SMD:SOT-23-3, F.Cu at (212.1, 6.76)
- added Q195: 2N3904, Package_TO_SOT_SMD:SOT-23-3, F.Cu at (212.1, 11.4)
- added Q196: 2N3904, Package_TO_SOT_SMD:SOT-23-3, F.Cu at (212.1, 16.0)
- added Q197: 2N3906, Package_TO_SOT_SMD:SOT-23-3, F.Cu at (217.2, -21.0)
- added Q198: 2N3904, Package_TO_SOT_SMD:SOT-23-3, F.Cu at (217.2, -16.4)
- added Q199: 2N3904, Package_TO_SOT_SMD:SOT-23-3, F.Cu at (217.2, -11.7)
- added Q200: 2N3904, Package_TO_SOT_SMD:SOT-23-3, F.Cu at (217.2, -7.11)
- added Q201: 2N3904, Package_TO_SOT_SMD:SOT-23-3, F.Cu at (217.2, -2.48)
- added Q202: 2N3904, Package_TO_SOT_SMD:SOT-23-3, F.Cu at (217.2, 2.14)
- added Q203: 2N3906, Package_TO_SOT_SMD:SOT-23-3, F.Cu at (217.2, 6.76)
- added Q204: 2N3904, Package_TO_SOT_SMD:SOT-23-3, F.Cu at (217.2, 11.4)
- added Q205: 2N3906, Package_TO_SOT_SMD:SOT-23-3, F.Cu at (217.2, 16.0)
- added Q206: 2N3904, Package_TO_SOT_SMD:SOT-23-3, F.Cu at (222.4, -21.0)
- added Q207: 2N3906, Package_TO_SOT_SMD:SOT-23-3, F.Cu at (222.4, -16.4)
- added Q208: 2N3904, Package_TO_SOT_SMD:SOT-23-3, F.Cu at (222.4, -11.7)
- added Q209: 2N3906, Package_TO_SOT_SMD:SOT-23-3, F.Cu at (222.4, -7.11)
- added Q210: 2N3906, Package_TO_SOT_SMD:SOT-23-3, F.Cu at (222.4, -2.48)
- added Q211: 2N3906, Package_TO_SOT_SMD:SOT-23-3, F.Cu at (222.4, 2.14)
- added Q212: 2N3904, Package_TO_SOT_SMD:SOT-23-3, F.Cu at (222.4, 6.76)
- added Q213: 2N3906, Package_TO_SOT_SMD:SOT-23-3, F.Cu at (222.4, 11.4)
- added Q214: 2N3906, Package_TO_SOT_SMD:SOT-23-3, F.Cu at (222.4, 16.0)
- added Q215: 2N3906, Package_TO_SOT_SMD:SOT-23-3, F.Cu at (227.6, -21.0)
- added Q216: 2N3906, Package_TO_SOT_SMD:SOT-23-3, F.Cu at (227.6, -16.4)
- added Q217: 2N3904, Package_TO_SOT_SMD:SOT-23-3, F.Cu at (227.6, -11.7)
- added Q218: 2N3906, Package_TO_SOT_SMD:SOT-23-3, F.Cu at (227.6, -7.11)
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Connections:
- D10 pad 1: /OUT_C1 -> Net-(D10-A)
- D11 pad 3: /OUT_S0 -> Net-(D11-K)
- D3 pad 3: /A0 -> Net-(D3-K)
- D4 pad 3: /B0 -> Net-(D4-K)
- D5 pad 1: Net-(D5-A) -> /alu_5/C1
- D6 pad 1: /~{OUT_G0} -> /alu_5/C2
- D7 pad 1: Net-(D7-A) -> /alu_5/C3
- D7 pad 3: /OUT_P0 -> Net-(D7-K)
- D8 pad 1: Net-(D8-A) -> /C8
- Q1 pad 1: VCC -> 0
- Q1 pad 2: /IN_A0 -> /alu_5/OUT_P0
- Q10 pad 1: 0 -> VCC
- Q10 pad 2: /IN_INV_B -> Net-(Q10-B)
- Q12 pad 2: Net-(Q10-E) -> Net-(Q12-B)
- Q13 pad 2: Net-(D1-K) -> /alu_5/OUT_G0
- Q13 pad 3: Net-(Q11-E) -> Net-(Q13-E)
- Q14 pad 2: Net-(D2-K) -> /alu_5/OUT_G1
- Q14 pad 3: Net-(Q12-E) -> Net-(Q10-E)
- Q15 pad 1: /A0 -> VCC
- Q15 pad 2: Net-(D3-A) -> /alu_5/OUT_G2
- Q15 pad 3: 0 -> Net-(Q11-E)
- Q16 pad 1: /B0 -> VCC
- Q16 pad 2: Net-(D4-A) -> /alu_5/OUT_G3
- Q16 pad 3: 0 -> Net-(Q12-E)
- Q17 pad 2: AND_EN -> /IN_C_IS_1
- Q17 pad 3: Net-(Q17-E) -> Net-(Q13-E)
- Q18 pad 1: 0 -> VCC
- Q18 pad 2: ~{IN_C_IS_0} -> /IN_C_IS_1
- Q18 pad 3: Net-(Q18-E) -> Net-(Q10-E)
- Q19 pad 2: /A0 -> /IN_C_IS_1
- Q19 pad 3: Net-(Q17-E) -> Net-(Q11-E)
- Q2 pad 1: VCC -> 0
- Q2 pad 2: /IN_B0 -> /alu_5/OUT_P1
- Q2 pad 3: Net-(Q2-E) -> Net-(Q10-B)
- Q20 pad 1: 0 -> VCC
- Q20 pad 2: /A0 -> /IN_C_IS_1
- Q20 pad 3: Net-(Q18-E) -> Net-(Q12-E)
- Q21 pad 1: VCC -> Net-(D1-K)
- Q21 pad 2: /B0 -> Net-(D1-A)
- Q21 pad 3: Net-(Q17-E) -> 0
- Q22 pad 1: 0 -> Net-(D2-K)
- Q22 pad 2: /B0 -> Net-(D2-A)
- Q22 pad 3: Net-(Q18-E) -> 0
- Q23 pad 1: Net-(D5-K) -> Net-(D3-K)
- Q23 pad 2: Net-(D5-A) -> Net-(D3-A)
- Q24 pad 1: /~{OUT_G0} -> Net-(D4-K)
- Q24 pad 2: Net-(D6-K) -> Net-(D4-A)
- Q24 pad 3: VCC -> 0
- Q25 pad 1: 0 -> /alu_5/C1
- Q25 pad 2: /A0 -> Net-(D5-K)
- Q25 pad 3: Net-(Q25-E) -> VCC
- Q26 pad 1: 0 -> /alu_5/C2
- Q26 pad 2: /B0 -> Net-(D6-K)
- Q26 pad 3: Net-(Q25-E) -> VCC
- Q27 pad 1: 0 -> /alu_5/C3
- Q27 pad 2: ~{OR_EN} -> Net-(D7-K)
- Q27 pad 3: Net-(Q25-E) -> VCC
- Q28 pad 1: VCC -> /C8
- Q28 pad 2: Net-(Q25-E) -> Net-(D8-K)
- Q28 pad 3: Net-(Q28-E) -> VCC
- Q29 pad 2: Net-(D5-K) -> /A7
- Q29 pad 3: Net-(Q28-E) -> Net-(Q29-E)
- Q3 pad 1: VCC -> 0
- Q3 pad 2: /IN_INV_A -> /alu_5/OUT_P2
- Q3 pad 3: Net-(Q1-E) -> Net-(Q11-B)
- Q30 pad 1: /OUT_P0 -> VCC
- Q30 pad 2: Net-(D7-A) -> /B7
- Q30 pad 3: 0 -> Net-(Q30-E)
- Q31 pad 1: 0 -> VCC
- Q31 pad 2: /IN_C0 -> /IN_INV_A
- Q31 pad 3: Net-(Q31-E) -> Net-(Q29-E)
- Q32 pad 1: 0 -> VCC
- Q32 pad 2: /OUT_P0 -> /IN_INV_B
- Q32 pad 3: Net-(Q31-E) -> Net-(Q30-E)
- Q33 pad 1: VCC -> Net-(D9-K)
- Q33 pad 2: /IN_C0 -> Net-(D9-A)
- Q33 pad 3: Net-(Q33-E) -> 0
- Q34 pad 1: VCC -> Net-(D10-K)
- Q34 pad 2: /OUT_P0 -> Net-(D10-A)
- Q34 pad 3: Net-(Q33-E) -> 0
- Q35 pad 1: Net-(D8-A) -> VCC
- Q35 pad 2: Net-(D8-K) -> /alu_5/C3
- Q35 pad 3: VCC -> Net-(Q35-E)
- Q36 pad 1: Net-(D9-K) -> VCC
- Q36 pad 2: Net-(D9-A) -> /alu_5/OUT_P3
- Q36 pad 3: 0 -> Net-(Q35-E)
- Q37 pad 2: ~{IN_C_IS_1} -> /A7
- Q38 pad 2: /~{OUT_G0} -> /B7
- Q38 pad 3: Net-(Q37-E) -> Net-(Q38-E)
- Q39 pad 2: /IN_C0 -> /IN_INV_A
- Q39 pad 3: Net-(Q39-E) -> Net-(Q37-E)
- Q4 pad 1: VCC -> 0
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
